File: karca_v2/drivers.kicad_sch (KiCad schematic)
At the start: 13 parts, among them J10 Screw_Terminal_01x04, J11 Buzzer, J9 Screw_Terminal_01x10, Q4 AO3400A

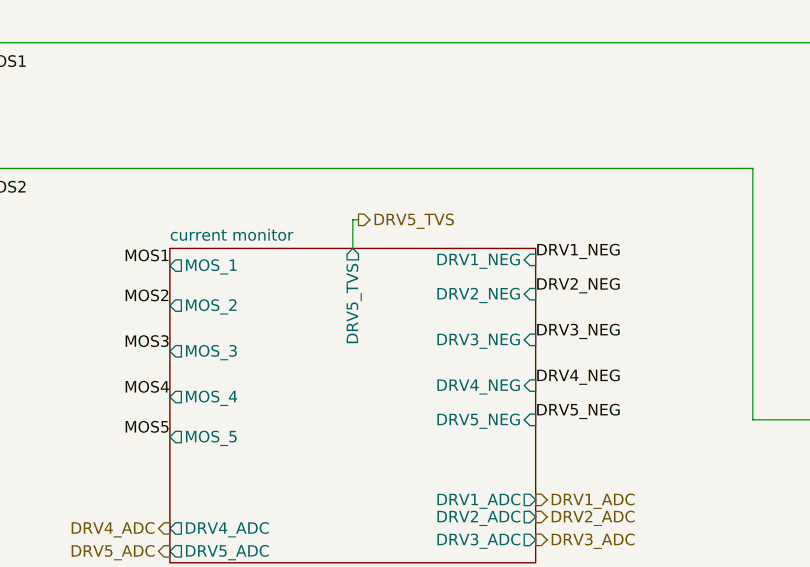
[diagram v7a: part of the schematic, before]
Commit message: fixed all routing. Now need to clean up vias
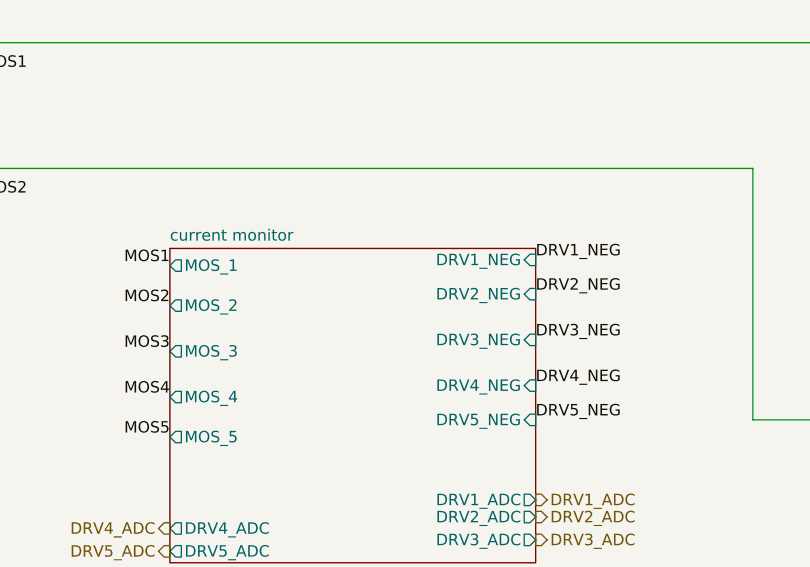
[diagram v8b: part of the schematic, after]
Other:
- sheet current monitor ports: added none; removed DRV5_TVS
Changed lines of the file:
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@@
-	(wire
-		(pts
-			(xy 124.46 41.275) (xy 124.46 44.45)
-		)
-		(stroke
-			(width 0)
-			(type default)
-		)
-	)
 	(wire
 		(pts
@@
 		(pts
 			(xy 232.41 58.42) (xy 232.41 21.59)
-		)
-		(stroke
-			(width 0)
-			(type default)
-		)
-	)
-	(wire
-		(pts
-			(xy 125.095 41.275) (xy 124.46 41.275)
 		)
 		(stroke
@@
 		(shape output)
 		(at 144.78 72.39 0)
-		(effects
-			(font
-				(size 1.27 1.27)
-			)
-			(justify left)
-		)
-	)
-	(hierarchical_label "DRV5_TVS"
-		(shape output)
-		(at 125.095 41.275 0)
 		(effects
 			(font
@@
 			(effects
 				(font
-					(size 1.27 1.27)
-				)
-				(justify right)
-			)
-		)
-		(pin "DRV5_TVS" output
-			(at 124.46 44.45 90)
-			(effects
-				(font
